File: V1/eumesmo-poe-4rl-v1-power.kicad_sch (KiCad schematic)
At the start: 31 parts, among them U4 TPS2376DDAR-H, U5 TX4138, U6 SY8089A1AAC

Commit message: Renamed all files to align with eumesmo branding.
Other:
- title: ESP 4x Relay Output Module with PoE -> eumesmo 4x Relay Output Module with PoE
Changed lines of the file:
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@@
 	(paper "A4")
 	(title_block
-		(title "ESP 4x Relay Output Module with PoE")
-		(date "2026-06-10")
+		(title "eumesmo 4x Relay Output Module with PoE")
+		(date "2026-06-16")
 		(rev "V1.0")
 	)
@@
 		)
 		(instances
-			(project "esp-poe-4rl-V1"
+			(project "eumesmo-poe-4rl-v1"
 				(path "/2bc5a21a-1d79-419d-a592-6852cc07b00a/2ac7b96d-5459-407c-a3e3-5692241632df"
 					(reference "#PWR063")
@@
 		)
 		(instances
-			(project "esp-poe-4rl-V1"
+			(project "eumesmo-poe-4rl-v1"
 				(path "/2bc5a21a-1d79-419d-a592-6852cc07b00a/2ac7b96d-5459-407c-a3e3-5692241632df"
 					(reference "R31")
@@
 		)
 		(instances
-			(project "esp-poe-4rl-V1"
+			(project "eumesmo-poe-4rl-v1"
 				(path "/2bc5a21a-1d79-419d-a592-6852cc07b00a/2ac7b96d-5459-407c-a3e3-5692241632df"
 					(reference "#PWR050")
@@
 		)
 		(instances
-			(project "esp-poe-4rl-V1"
+			(project "eumesmo-poe-4rl-v1"
 				(path "/2bc5a21a-1d79-419d-a592-6852cc07b00a/2ac7b96d-5459-407c-a3e3-5692241632df"
 					(reference "C23")
@@
 		)
 		(instances
-			(project "esp-poe-4rl-V1"
+			(project "eumesmo-poe-4rl-v1"
 				(path "/2bc5a21a-1d79-419d-a592-6852cc07b00a/2ac7b96d-5459-407c-a3e3-5692241632df"
 					(reference "R34")
@@
 		)
 		(instances
-			(project "esp-poe-4rl-V1"
+			(project "eumesmo-poe-4rl-v1"
 				(path "/2bc5a21a-1d79-419d-a592-6852cc07b00a/2ac7b96d-5459-407c-a3e3-5692241632df"
 					(reference "#PWR057")
@@
 		)
 		(instances
-			(project "esp-poe-4rl-V1"
+			(project "eumesmo-poe-4rl-v1"
 				(path "/2bc5a21a-1d79-419d-a592-6852cc07b00a/2ac7b96d-5459-407c-a3e3-5692241632df"
 					(reference "L3")
@@
 		)
 		(instances
-			(project "esp-poe-4rl-V1"
+			(project "eumesmo-poe-4rl-v1"
 				(path "/2bc5a21a-1d79-419d-a592-6852cc07b00a/2ac7b96d-5459-407c-a3e3-5692241632df"
 					(reference "C21")
@@
 		)
 		(instances
-			(project "esp-poe-4rl-V1"
+			(project "eumesmo-poe-4rl-v1"
 				(path "/2bc5a21a-1d79-419d-a592-6852cc07b00a/2ac7b96d-5459-407c-a3e3-5692241632df"
 					(reference "C27")
@@
 		)
 		(instances
-			(project "esp-poe-4rl-V1"
+			(project "eumesmo-poe-4rl-v1"
 				(path "/2bc5a21a-1d79-419d-a592-6852cc07b00a/2ac7b96d-5459-407c-a3e3-5692241632df"
 					(reference "#PWR055")
@@
 		)
 		(instances
-			(project "esp-poe-4rl-V1"
+			(project "eumesmo-poe-4rl-v1"
 				(path "/2bc5a21a-1d79-419d-a592-6852cc07b00a/2ac7b96d-5459-407c-a3e3-5692241632df"
 					(reference "#PWR060")
@@
 		)
 		(instances
-			(project "esp-poe-4rl-V1"
+			(project "eumesmo-poe-4rl-v1"
 				(path "/2bc5a21a-1d79-419d-a592-6852cc07b00a/2ac7b96d-5459-407c-a3e3-5692241632df"
 					(reference "D5")
@@
 		)
 		(instances
-			(project "esp-poe-4rl-V1"
+			(project "eumesmo-poe-4rl-v1"
 				(path "/2bc5a21a-1d79-419d-a592-6852cc07b00a/2ac7b96d-5459-407c-a3e3-5692241632df"
 					(reference "R26")
@@
 		)
 		(instances
-			(project "esp-poe-4rl-V1"
+			(project "eumesmo-poe-4rl-v1"
 				(path "/2bc5a21a-1d79-419d-a592-6852cc07b00a/2ac7b96d-5459-407c-a3e3-5692241632df"
 					(reference "L2")
@@
 		)
 		(instances
-			(project "esp-poe-4rl-V1"
+			(project "eumesmo-poe-4rl-v1"
 				(path "/2bc5a21a-1d79-419d-a592-6852cc07b00a/2ac7b96d-5459-407c-a3e3-5692241632df"
 					(reference "R29")
@@
 		)
 		(instances
-			(project "esp-poe-4rl-V1"
+			(project "eumesmo-poe-4rl-v1"
 				(path "/2bc5a21a-1d79-419d-a592-6852cc07b00a/2ac7b96d-5459-407c-a3e3-5692241632df"
 					(reference "C26")
@@
 		)
 		(instances
-			(project "esp-poe-4rl-V1"
+			(project "eumesmo-poe-4rl-v1"
 				(path "/2bc5a21a-1d79-419d-a592-6852cc07b00a/2ac7b96d-5459-407c-a3e3-5692241632df"
 					(reference "U4")
@@
 		)
 		(instances
-			(project "esp-poe-4rl-V1"
+			(project "eumesmo-poe-4rl-v1"
 				(path "/2bc5a21a-1d79-419d-a592-6852cc07b00a/2ac7b96d-5459-407c-a3e3-5692241632df"
 					(reference "C22")
@@
 		)
 		(instances
-			(project "esp-poe-4rl-V1"
+			(project "eumesmo-poe-4rl-v1"
 				(path "/2bc5a21a-1d79-419d-a592-6852cc07b00a/2ac7b96d-5459-407c-a3e3-5692241632df"
 					(reference "#FLG05")
@@
 		)
 		(instances
-			(project "esp-poe-4rl-V1"
+			(project "eumesmo-poe-4rl-v1"
 				(path "/2bc5a21a-1d79-419d-a592-6852cc07b00a/2ac7b96d-5459-407c-a3e3-5692241632df"
 					(reference "R27")
@@
 		)
 		(instances
-			(project "esp-poe-4rl-V1"
+			(project "eumesmo-poe-4rl-v1"
 				(path "/2bc5a21a-1d79-419d-a592-6852cc07b00a/2ac7b96d-5459-407c-a3e3-5692241632df"
 					(reference "#PWR053")
@@
 		)
 		(instances
-			(project "esp-poe-4rl-V1"
+			(project "eumesmo-poe-4rl-v1"
 				(path "/2bc5a21a-1d79-419d-a592-6852cc07b00a/2ac7b96d-5459-407c-a3e3-5692241632df"
 					(reference "D4")
@@
 		)
 		(instances
-			(project "esp-poe-4rl-V1"
+			(project "eumesmo-poe-4rl-v1"
 				(path "/2bc5a21a-1d79-419d-a592-6852cc07b00a/2ac7b96d-5459-407c-a3e3-5692241632df"
 					(reference "#PWR059")
@@
 		)
 		(instances
-			(project "esp-poe-4rl-V1"
+			(project "eumesmo-poe-4rl-v1"
 				(path "/2bc5a21a-1d79-419d-a592-6852cc07b00a/2ac7b96d-5459-407c-a3e3-5692241632df"
 					(reference "R25")
@@
 		)
 		(instances
-			(project "esp-poe-4rl-V1"
+			(project "eumesmo-poe-4rl-v1"
 				(path "/2bc5a21a-1d79-419d-a592-6852cc07b00a/2ac7b96d-5459-407c-a3e3-5692241632df"
 					(reference "#PWR052")
@@
 		)
 		(instances
-			(project "esp-poe-4rl-V1"
+			(project "eumesmo-poe-4rl-v1"
 				(path "/2bc5a21a-1d79-419d-a592-6852cc07b00a/2ac7b96d-5459-407c-a3e3-5692241632df"
 					(reference "R33")
@@
 		)
 		(instances
-			(project "esp-poe-4rl-V1"
+			(project "eumesmo-poe-4rl-v1"
 				(path "/2bc5a21a-1d79-419d-a592-6852cc07b00a/2ac7b96d-5459-407c-a3e3-5692241632df"
 					(reference "R35")
@@
 		)
 		(instances
-			(project "esp-poe-4rl-V1"
+			(project "eumesmo-poe-4rl-v1"
 				(path "/2bc5a21a-1d79-419d-a592-6852cc07b00a/2ac7b96d-5459-407c-a3e3-5692241632df"
 					(reference "R30")
@@
 		)
 		(instances
-			(project "esp-poe-4rl-V1"
+			(project "eumesmo-poe-4rl-v1"
 				(path "/2bc5a21a-1d79-419d-a592-6852cc07b00a/2ac7b96d-5459-407c-a3e3-5692241632df"
 					(reference "R32")
@@
 		)
 		(instances
-			(project "esp-poe-4rl-V1"
+			(project "eumesmo-poe-4rl-v1"
 				(path "/2bc5a21a-1d79-419d-a592-6852cc07b00a/2ac7b96d-5459-407c-a3e3-5692241632df"
 					(reference "R28")
@@
 		)
 		(instances
-			(project "esp-poe-4rl-V1"
+			(project "eumesmo-poe-4rl-v1"
 				(path "/2bc5a21a-1d79-419d-a592-6852cc07b00a/2ac7b96d-5459-407c-a3e3-5692241632df"
 					(reference "D3")
@@
 		)
 		(instances
-			(project "esp-poe-4rl-V1"
+			(project "eumesmo-poe-4rl-v1"
 				(path "/2bc5a21a-1d79-419d-a592-6852cc07b00a/2ac7b96d-5459-407c-a3e3-5692241632df"
 					(reference "D7")
@@
 		)
 		(instances
-			(project "esp-poe-4rl-V1"
+			(project "eumesmo-poe-4rl-v1"
 				(path "/2bc5a21a-1d79-419d-a592-6852cc07b00a/2ac7b96d-5459-407c-a3e3-5692241632df"
 					(reference "R36")
@@
 		)
 		(instances
-			(project "esp-poe-4rl-V1"
+			(project "eumesmo-poe-4rl-v1"
 				(path "/2bc5a21a-1d79-419d-a592-6852cc07b00a/2ac7b96d-5459-407c-a3e3-5692241632df"
 					(reference "U5")
@@
 		)
 		(instances
-			(project "esp-poe-4rl-V1"
+			(project "eumesmo-poe-4rl-v1"
 				(path "/2bc5a21a-1d79-419d-a592-6852cc07b00a/2ac7b96d-5459-407c-a3e3-5692241632df"
 					(reference "#PWR056")
@@
 		)
 		(instances
-			(project "esp-poe-4rl-V1"
+			(project "eumesmo-poe-4rl-v1"
 				(path "/2bc5a21a-1d79-419d-a592-6852cc07b00a/2ac7b96d-5459-407c-a3e3-5692241632df"
 					(reference "R37")
@@
 		)
 		(instances
-			(project "esp-poe-4rl-V1"
+			(project "eumesmo-poe-4rl-v1"
 				(path "/2bc5a21a-1d79-419d-a592-6852cc07b00a/2ac7b96d-5459-407c-a3e3-5692241632df"
 					(reference "#PWR054")
@@
 		)
 		(instances
-			(project "esp-poe-4rl-V1"
+			(project "eumesmo-poe-4rl-v1"
 				(path "/2bc5a21a-1d79-419d-a592-6852cc07b00a/2ac7b96d-5459-407c-a3e3-5692241632df"
 					(reference "#PWR062")
@@
 		)
 		(instances
-			(project "esp-poe-4rl-V1"
+			(project "eumesmo-poe-4rl-v1"
 				(path "/2bc5a21a-1d79-419d-a592-6852cc07b00a/2ac7b96d-5459-407c-a3e3-5692241632df"
 					(reference "C24")
@@
 		)
 		(instances
-			(project "esp-poe-4rl-V1"
+			(project "eumesmo-poe-4rl-v1"
 				(path "/2bc5a21a-1d79-419d-a592-6852cc07b00a/2ac7b96d-5459-407c-a3e3-5692241632df"
 					(reference "U6")
@@
 		)
 		(instances
-			(project "esp-poe-4rl-V1"
+			(project "eumesmo-poe-4rl-v1"
 				(path "/2bc5a21a-1d79-419d-a592-6852cc07b00a/2ac7b96d-5459-407c-a3e3-5692241632df"
 					(reference "#PWR061")
@@
 		)
 		(instances
-			(project "esp-poe-4rl-V1"
+			(project "eumesmo-poe-4rl-v1"
 				(path "/2bc5a21a-1d79-419d-a592-6852cc07b00a/2ac7b96d-5459-407c-a3e3-5692241632df"
 					(reference "C25")
@@
 		)
 		(instances
-			(project "esp-poe-4rl-V1"
+			(project "eumesmo-poe-4rl-v1"
 				(path "/2bc5a21a-1d79-419d-a592-6852cc07b00a/2ac7b96d-5459-407c-a3e3-5692241632df"
 					(reference "D6")
@@
 		)
 		(instances
-			(project "esp-poe-4rl-V1"
+			(project "eumesmo-poe-4rl-v1"
 				(path "/2bc5a21a-1d79-419d-a592-6852cc07b00a/2ac7b96d-5459-407c-a3e3-5692241632df"
 					(reference "#PWR051")
@@
 		)
 		(instances
-			(project "esp-poe-4rl-V1"
+			(project "eumesmo-poe-4rl-v1"
 				(path "/2bc5a21a-1d79-419d-a592-6852cc07b00a/2ac7b96d-5459-407c-a3e3-5692241632df"
 					(reference "C28")
@@
 		)
 		(instances
-			(project "esp-poe-4rl-V1"
+			(project "eumesmo-poe-4rl-v1"
 				(path "/2bc5a21a-1d79-419d-a592-6852cc07b00a/2ac7b96d-5459-407c-a3e3-5692241632df"
 					(reference "#PWR058")
@@
 		)
 		(instances
-			(project "esp-poe-4rl-V1"
+			(project "eumesmo-poe-4rl-v1"
 				(path "/2bc5a21a-1d79-419d-a592-6852cc07b00a/2ac7b96d-5459-407c-a3e3-5692241632df"
 					(reference "#FLG04")

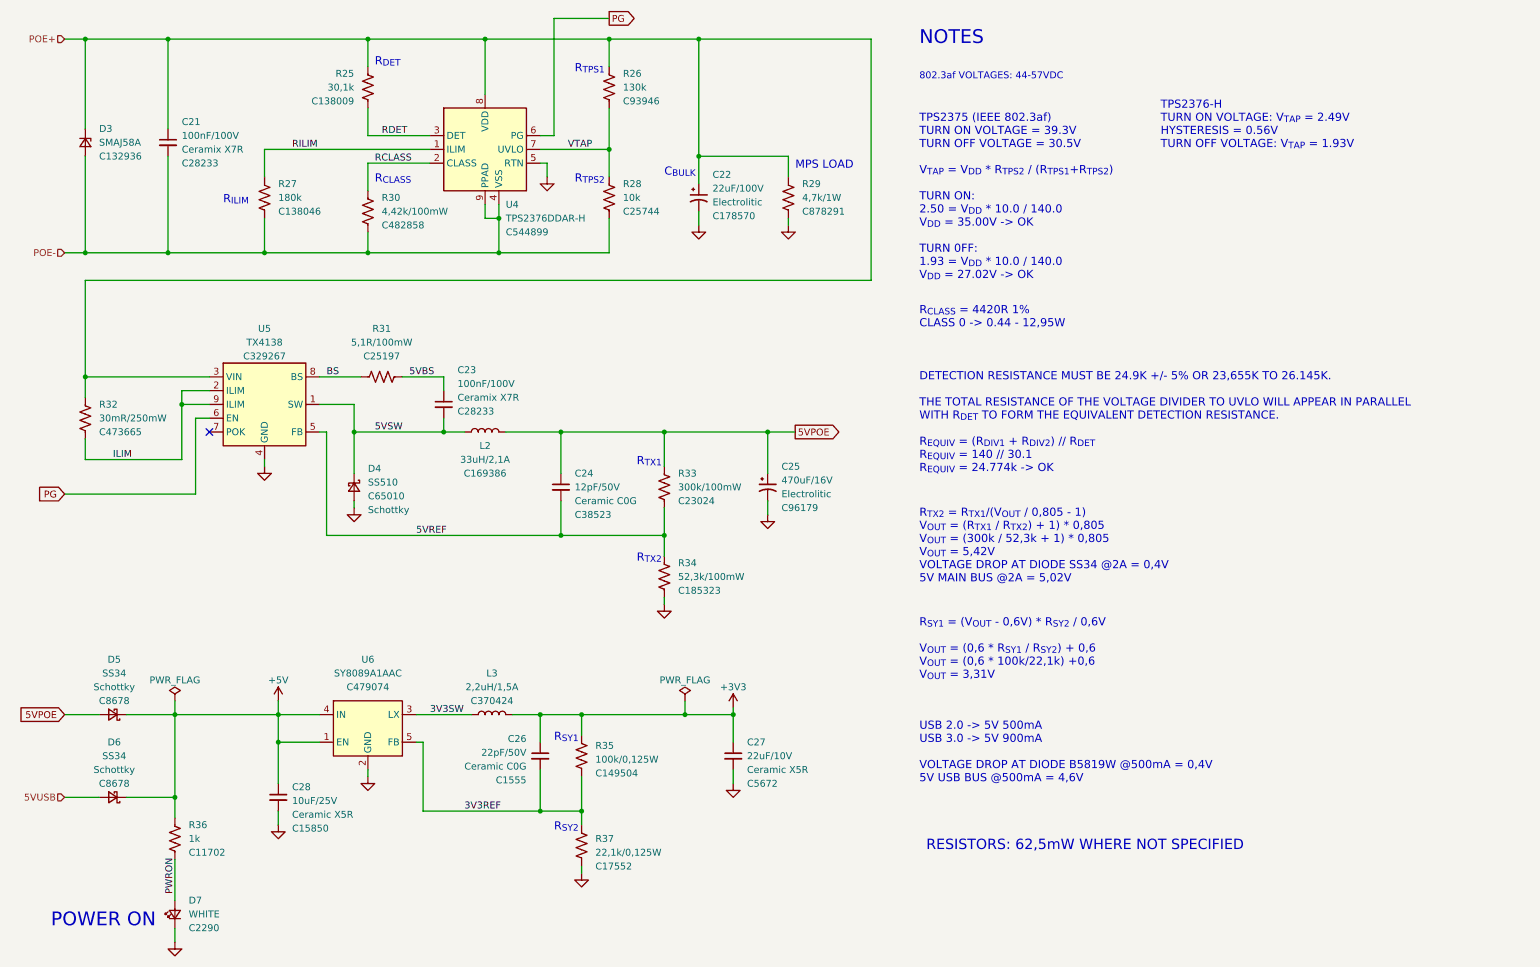
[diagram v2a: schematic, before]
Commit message: Added CPU health LED
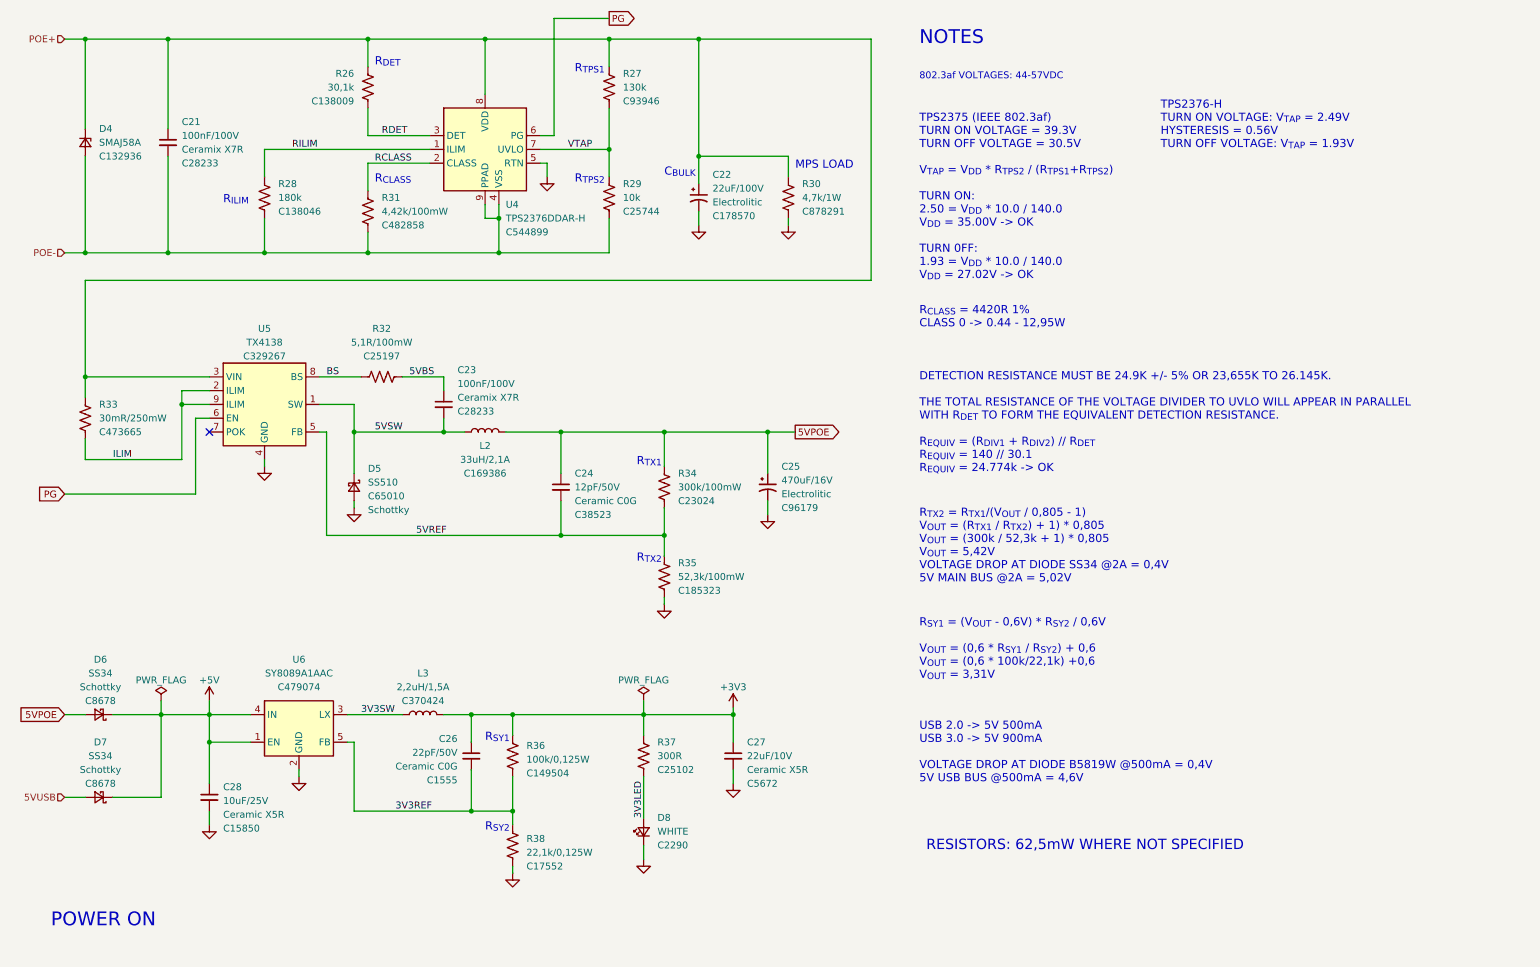
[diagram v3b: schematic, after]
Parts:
- removed D7: WHITE, Tales:LED_0603_1608Metric, symbol Device:LED_Small
- removed R36: 1k, Tales:R_0402_1005Metric, symbol Device:R_US
- added D8: WHITE, Tales:LED_0603_1608Metric, symbol Device:LED_Small
- added R37: 300R, Tales:R_0402_1005Metric, symbol Device:R_US
- renumbered D3 to D4, D4 to D5, D5 to D6, D6 to D7, R25 to R26, R26 to R27, R27 to R28, R28 to R29, R29 to R30, R30 to R31, R31 to R32, R32 to R33, R33 to R34, R34 to R35, R35 to R36, R37 to R38
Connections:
- net +3V3: now also R37.1
- net GND: now also D8.1 (K)
- new net 3V3LED: D8.2 (A), R37.2
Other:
- moved on the sheet: C26, C28, D6, D7, L3, R36, R38, U6
